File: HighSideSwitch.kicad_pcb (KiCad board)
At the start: 2 copper layers, 22 x 15.1 mm, 22 parts, among them J1 Conn_02x02_Odd_Even, Q1 CSD18540Q5B, Q2 8050, Q3 8050, U1 BTS443P, U2 LM5050-1

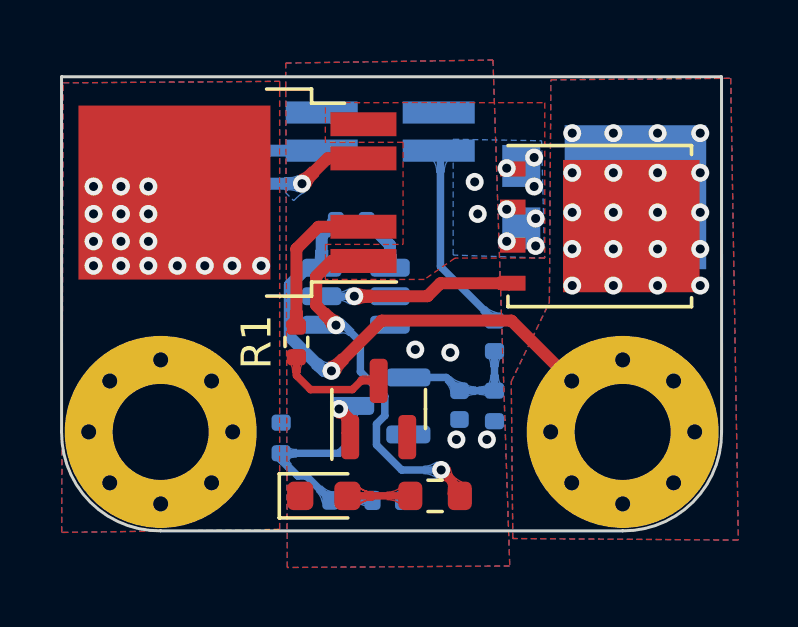
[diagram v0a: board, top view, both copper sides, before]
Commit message: Use LM5060 as high side switch instead BTS443P
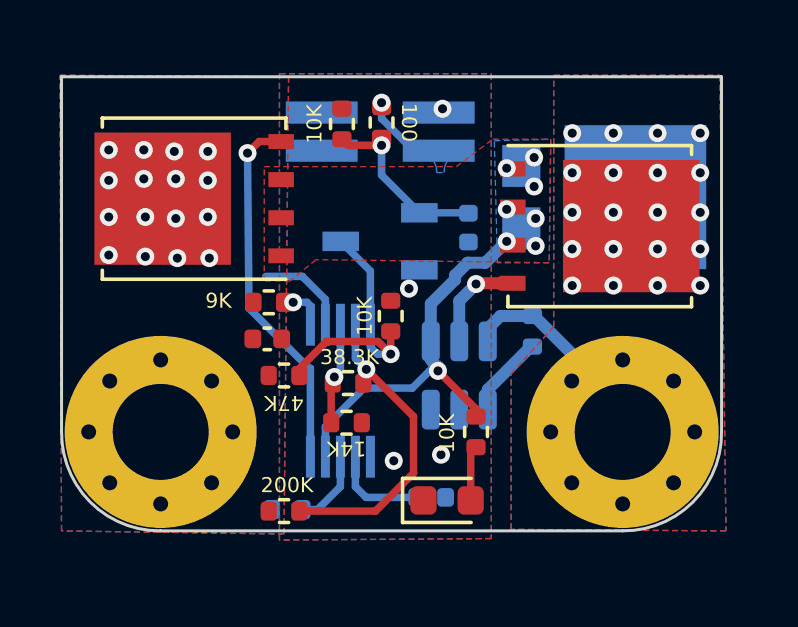
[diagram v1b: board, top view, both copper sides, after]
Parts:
- removed C2: 100n, Capacitor_SMD:C_0402_1005Metric
- removed D3: LED, LED_SMD:LED_0603_1608Metric
- added C3: 100n, Capacitor_SMD:C_0402_1005Metric, B.Cu at (188.5, 93.6)
- added C4: 100n, Capacitor_SMD:C_0402_1005Metric, B.Cu at (189.7, 84.6)
- added R10: 10K, Resistor_SMD:R_0402_1005Metric, F.Cu at (185.5, 81.1)
- added R11: 10K, Resistor_SMD:R_0402_1005Metric, F.Cu at (190.0, 91.4)
- C1: moved to F.Cu
- D2: value BZT52C12 -> LED; footprint Diode_SMD:D_SOD-123 -> LED_SMD:LED_0603_1608Metric; moved to F.Cu
- Q2: value 8050 -> CSD18540Q5B; footprint Package_TO_SOT_SMD:SOT-23 -> Package_TO_SOT_SMD:TDSON-8-1
- Q3: footprint Package_TO_SOT_SMD:SOT-23 -> Package_TO_SOT_SMD:TSOT-23
- R1: value 10K -> 9K
- R3: value 10K -> 200K; moved to F.Cu
- R4: value 10K -> 100K; footprint Resistor_SMD:R_0603_1608Metric -> Resistor_SMD:R_0402_1005Metric; moved to B.Cu
- R5: value 2K -> 38.3K; moved to F.Cu
- R6: value 10K -> 14K; moved to F.Cu
- R7: value 10K -> 47K; moved to F.Cu
- R8: value 100 -> 10K; moved to F.Cu
- R9: value 10K -> 100; moved to F.Cu
- U1: value BTS443P -> LM5060; footprint Package_TO_SOT_SMD:TO-252-4 -> Package_SO:MSOP-10_3x3mm_P0.5mm; moved to B.Cu
- moved D2 15.3 mm to (189.0, 93.7)
- moved R9 10.2 mm to (186.8, 81.1), turned to -90 degrees
- moved Q2 9.33 mm to (180.6, 83.6), turned to 180 degrees
- moved R6 8.45 mm to (185.7, 91.1), turned to 180 degrees
- moved U1 7.44 mm to (185.5, 90.0), turned to -90 degrees
- moved R2 7.06 mm to (191.9, 88.0), turned to 90 degrees
- moved R5 6.26 mm to (185.7, 89.8)
- moved C1 5.63 mm to (183.0, 88.3), turned to 0 degrees
- moved Q3 5.49 mm to (186.8, 85.0)
- moved R7 5.41 mm to (183.6, 89.5), turned to 0 degrees
- moved R4 4.95 mm to (183.7, 94.0)
- moved U2 4.34 mm to (189.4, 89.5), turned to 90 degrees
- moved R8 3.52 mm to (187.1, 87.5)
- moved R3 2.44 mm to (183.6, 94.0), turned to 0 degrees
- moved R1 1.61 mm to (183.1, 87.1), turned to 0 degrees
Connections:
- C1 pad 1: Net-(C1-Pad1) -> /NMOS_IN
- D2 pad 1: Net-(D2-Pad1) -> GND
- D2 pad 2: GND -> Net-(D2-Pad2)
- Q2 pad 1: Net-(C1-Pad1) -> Net-(D1-Pad1)
- Q2 pad 2: GND -> Net-(D1-Pad1)
- Q2 pad 3: Net-(Q2-Pad3) -> Net-(D1-Pad1)
- Q3 pad 1: Net-(C2-Pad1) -> Net-(C4-Pad1)
- Q3 pad 3: Net-(C1-Pad1) -> /EN
- R1 pad 1: Net-(Q2-Pad3) -> /NMOS_IN
- R3 pad 1: Net-(C1-Pad1) -> /NMOS_IN
- R3 pad 2: /NMOS_IN -> Net-(R3-Pad2)
- R4 pad 1: Net-(D3-Pad2) -> /NMOS_IN
- R4 pad 2: Net-(D1-Pad1) -> Net-(R4-Pad2)
- R5 pad 1: Net-(D2-Pad1) -> Net-(R5-Pad1)
- R5 pad 2: Net-(R5-Pad2) -> Net-(R3-Pad2)
- R6 pad 2: Net-(R5-Pad2) -> Net-(R5-Pad1)
- R7 pad 1: GND -> /NMOS_IN
- R7 pad 2: Net-(C1-Pad1) -> /EN
- R8 pad 1: Net-(C2-Pad1) -> /EN
- R8 pad 2: /~{EN} -> GND
- R9 pad 1: GND -> /~{EN}
- R9 pad 2: Net-(C2-Pad1) -> Net-(C4-Pad1)
- U1 pad 1: Net-(D1-Pad1) -> Net-(R1-Pad2)
- U1 pad 2: Net-(R1-Pad2) -> /NMOS_IN
- U1 pad 3: /NMOS_IN -> Net-(R5-Pad1)
- U1 pad 4: Net-(R5-Pad2) -> Net-(R3-Pad2)
- U1 pad 5: Net-(D1-Pad1) -> /EN
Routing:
- net Net-(Q2-Pad4): track 0.00 -> 12.3 mm, vias 0 -> 1
- net /NMOS_OUT: track 18.6 -> 7.23 mm, vias 21 -> 20
- net Net-(R3-Pad2): track 0.00 -> 10.1 mm, vias 0 -> 1
- net /EN: track 0.00 -> 9.29 mm, vias 0 -> 1
- net Net-(C1-Pad1): track 8.86 -> 0.00 mm, vias 1 -> 0
- net Net-(C4-Pad1): track 0.00 -> 5.82 mm, vias 0 -> 1
- net GND: track 5.70 -> 0.00 mm
- net Net-(D2-Pad1): track 5.54 -> 0.00 mm
- net Net-(R5-Pad2): track 5.30 -> 0.00 mm, vias 1 -> 0
- net Net-(C2-Pad1): track 4.37 -> 0.00 mm
- net /~{EN}: track 6.41 -> 2.04 mm, vias 0 -> 1
- net Net-(R1-Pad2): track 5.13 -> 1.25 mm, vias 0 -> 1
- net Net-(Q2-Pad3): track 3.67 -> 0.00 mm
- net Net-(C3-Pad1): track 0.00 -> 3.19 mm
- net Net-(Q1-Pad4): track 6.55 -> 3.38 mm
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
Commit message: reset
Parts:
- removed D2: LED, LED_SMD:LED_0603_1608Metric
- added D3: LED, GENERAL_2-PIN_PLASTIC_SMD:LED0603(1608M), F.Cu at (189.3, 93.9)
- C1, C3, C4: footprint Capacitor_SMD:C_0402_1005Metric -> GENERAL_RCL_SMD:C0402(1005M)
- D1: value VS-6ESU06 -> Diode; footprint Package_TO_SOT_SMD:TO-277A -> POWER_DIODE_SMD:TO-277A
- H1, H2: value MountingHole_Pad -> MountingHole; footprint MountingHole:MountingHole_3.2mm_M3_Pad_Via -> MOUNTINGHOLE:MountingHole
- J1: value Conn_02x02_Odd_Even -> Conn_02x02; footprint Connector_PinHeader_1.27mm:PinHeader_2x02_P1.27mm_Vertical_SMD -> CONNECTOR:Conn-02x02
- Q1, Q2: value CSD18540Q5B -> CSD18540; footprint Package_TO_SOT_SMD:TDSON-8-1 -> POWER_TRANSISTOR_SMD:SON-6050-FET
- Q3: footprint Package_TO_SOT_SMD:TSOT-23 -> GENERAL_SMALL-SEMI_SMD:SOT-23
- R1, R10, R11, R2, R3, R4, R5, R6, R7, R8, R9: footprint Resistor_SMD:R_0402_1005Metric -> GENERAL_RCL_SMD:R0402(1005M)
- U1: footprint Package_SO:MSOP-10_3x3mm_P0.5mm -> GENERAL_MIDDLE-SEMI_SMD:MSOP-3030_10
- U2: footprint Package_TO_SOT_SMD:TSOT-23-6 -> GENERAL_SMALL-SEMI_SMD:SOT-23-6
- turned D1 to 180 degrees
- turned Q1 to -90 degrees
- turned Q2 to 90 degrees
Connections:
- C3 pad 1: Net-(C3-Pad1) -> GND
- C3 pad 2: GND -> Net-(C3-Pad2)
- C4 pad 1: Net-(C4-Pad1) -> GND
- C4 pad 2: GND -> Net-(C4-Pad2)
- H1 pad 1: /NMOS_IN -> (no net)
- H2 pad 1: /NMOS_OUT -> (no net)
- Q3 pad 1: Net-(C4-Pad1) -> Net-(C4-Pad2)
- R10 pad 1: Net-(C4-Pad1) -> GND
- R10 pad 2: GND -> Net-(C4-Pad2)
- R11 pad 1: Net-(D1-Pad1) -> Net-(D3-PadA)
- R11 pad 2: Net-(D2-Pad2) -> Net-(Q2-Pad2)
- R3 pad 1: /NMOS_IN -> Net-(R3-Pad1)
- R3 pad 2: Net-(R3-Pad2) -> /NMOS_IN
- R5 pad 1: Net-(R5-Pad1) -> Net-(R3-Pad1)
- R5 pad 2: Net-(R3-Pad2) -> Net-(R5-Pad2)
- R6 pad 2: Net-(R5-Pad1) -> Net-(R5-Pad2)
- R7 pad 1: /NMOS_IN -> /EN
- R7 pad 2: /EN -> /NMOS_IN
- R9 pad 2: Net-(C4-Pad1) -> Net-(C4-Pad2)
- U1 pad 10: Net-(Q2-Pad4) -> Net-(Q2-Pad1)
- U1 pad 3: Net-(R5-Pad1) -> Net-(R5-Pad2)
- U1 pad 4: Net-(R3-Pad2) -> Net-(R3-Pad1)
- U1 pad 7: Net-(C3-Pad1) -> Net-(C3-Pad2)
- U1 pad 9: Net-(D1-Pad1) -> Net-(Q2-Pad2)
- U2 pad 4: Net-(D1-Pad1) -> Net-(Q2-Pad2)
- U2 pad 5: Net-(Q1-Pad4) -> Net-(Q1-Pad1)
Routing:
- net Net-(D1-Pad1): track 13.5 -> 0.00 mm, vias 8 -> 0
- net /NMOS_OUT: track 7.23 -> 20.7 mm, vias 20 -> 28
- net Net-(R5-Pad2): track 0.00 -> 13.2 mm, vias 0 -> 2
- net GND: track 0.00 -> 12.4 mm, vias 4 -> 6
- net Net-(Q2-Pad4): track 12.3 -> 0.00 mm, vias 1 -> 0
- net Net-(Q2-Pad1): track 0.00 -> 12.3 mm, vias 0 -> 1
- net Net-(R3-Pad2): track 10.1 -> 0.00 mm, vias 1 -> 0
- net Net-(C4-Pad1): track 5.82 -> 0.00 mm, vias 1 -> 0
- net Net-(Q1-Pad4): track 3.38 -> 0.00 mm, vias 1 -> 0
- net Net-(C3-Pad1): track 3.19 -> 0.00 mm
- net Net-(R5-Pad1): track 3.17 -> 0.00 mm, vias 1 -> 0
- net Net-(Q2-Pad2): track 0.00 -> 1.85 mm
- net Net-(D2-Pad2): track 1.85 -> 0.00 mm
- added copper zone on B.Cu, net Net-(Q2-Pad2)
- added copper zone on F.Cu, net Net-(Q2-Pad2)
- removed copper zone on B.Cu, net Net-(D1-Pad1)
- removed copper zone on F.Cu, net Net-(D1-Pad1)

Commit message: final
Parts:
- removed D3: LED, GENERAL_2-PIN_PLASTIC_SMD:LED0603(1608M)
- added D2: Diode_LED, GENERAL_2-PIN_PLASTIC_SMD:LED0603(1608M), F.Cu at (189.0, 93.7)
- Q1, Q2: value CSD18540 -> CSD18540Q5B
- moved Q1 0.13 mm to (194.2, 84.5)
- turned C3 to 180 degrees
- turned C4 to 90 degrees
- turned Q3 to 0 degrees
- turned R10 to -90 degrees
- turned R11 to 90 degrees
- turned R3 to 180 degrees
- turned R5 to 180 degrees
- turned R7 to 180 degrees
- turned U2 to -90 degrees
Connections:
- H1 pad 1: (no net) -> /NMOS_IN
- H2 pad 1: (no net) -> /NMOS_OUT
- Q1 pad D: (no net) -> /NMOS_OUT
- Q1 pad G: (no net) -> Net-(Q1-PadG)
- Q1 pad S: (no net) -> Net-(D1-PadA)
- Q2 pad G: (no net) -> Net-(Q2-PadG)
- Q2 pad S: (no net) -> Net-(D1-PadA)
- R11 pad 2: Net-(Q2-Pad2) -> Net-(D1-PadA)
- U1 pad 10: Net-(Q2-Pad1) -> Net-(Q2-PadG)
- U1 pad 9: Net-(Q2-Pad2) -> Net-(D1-PadA)
- U2 pad 4: Net-(Q2-Pad2) -> Net-(D1-PadA)
- U2 pad 5: Net-(Q1-Pad1) -> Net-(Q1-PadG)
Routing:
- net Net-(D1-PadA): track 0.00 -> 13.5 mm, vias 0 -> 8
- net /NMOS_OUT: track 20.7 -> 7.23 mm, vias 28 -> 20
- net GND: track 12.4 -> 0.00 mm, vias 6 -> 4
- net Net-(Q2-PadG): track 0.00 -> 12.3 mm, vias 0 -> 1
- net Net-(Q2-Pad1): track 12.3 -> 0.00 mm, vias 1 -> 0
- net Net-(R5-Pad2): track 13.2 -> 3.17 mm, vias 2 -> 1
- net Net-(R3-Pad1): track 0.00 -> 10.1 mm, vias 0 -> 1
- net Net-(C4-Pad2): track 0.00 -> 5.82 mm, vias 0 -> 1
- net Net-(Q1-PadG): track 0.00 -> 3.38 mm, vias 0 -> 1
- net Net-(C3-Pad2): track 0.00 -> 3.19 mm
- net Net-(Q2-Pad2): track 1.85 -> 0.00 mm
- net Net-(D2-Pad2): track 0.00 -> 1.85 mm
- added copper zone on B.Cu, net Net-(D1-PadA)
- added copper zone on F.Cu, net Net-(D1-PadA)
- removed copper zone on B.Cu, net Net-(Q2-Pad2)
- removed copper zone on F.Cu, net Net-(Q2-Pad2)
